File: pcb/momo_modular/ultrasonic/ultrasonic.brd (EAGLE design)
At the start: 100 x 80 mm, 39 parts, among them U1 TDC1000, U2 TDC7200, U3 PIC16LF1847

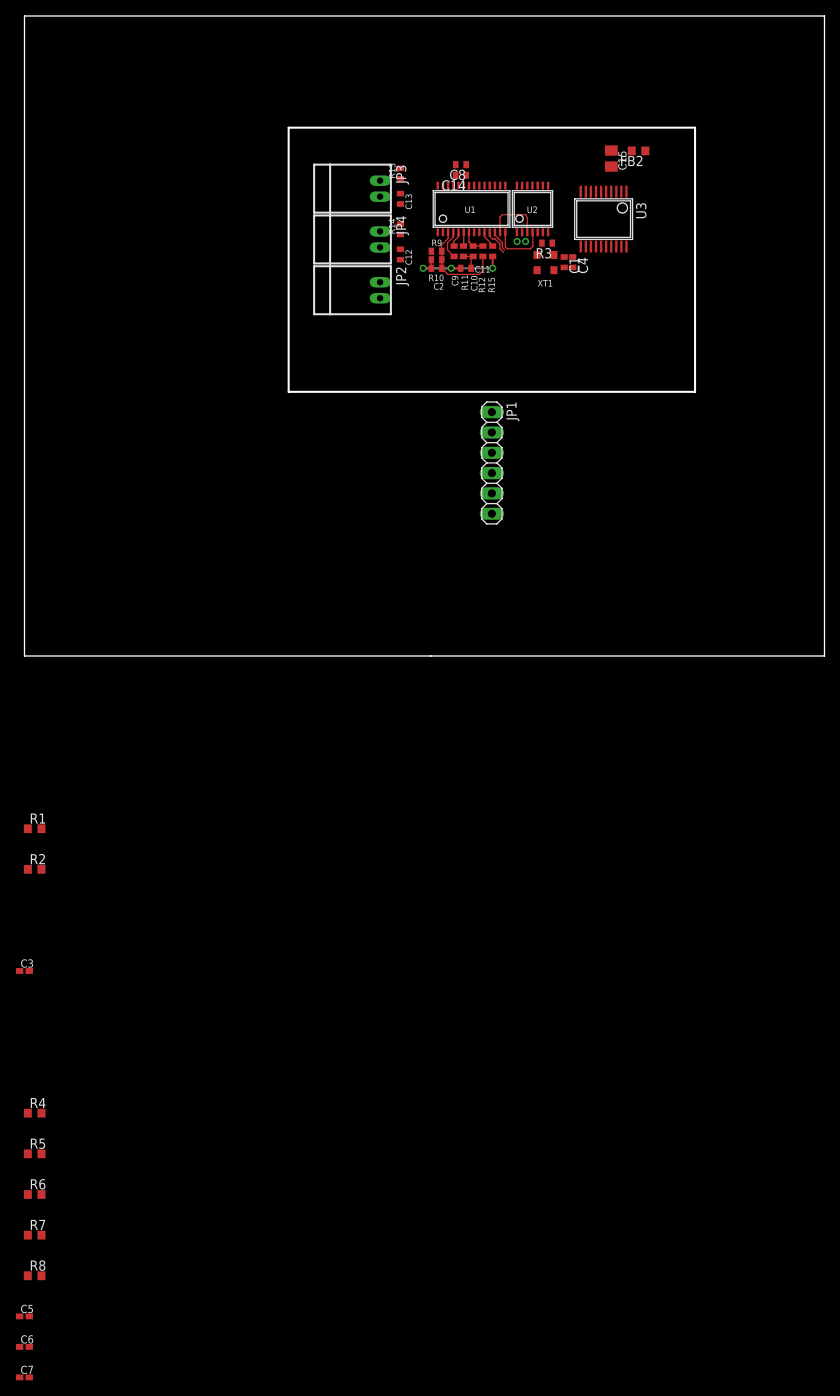
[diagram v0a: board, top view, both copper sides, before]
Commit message: Continue layout of ultrasonic board
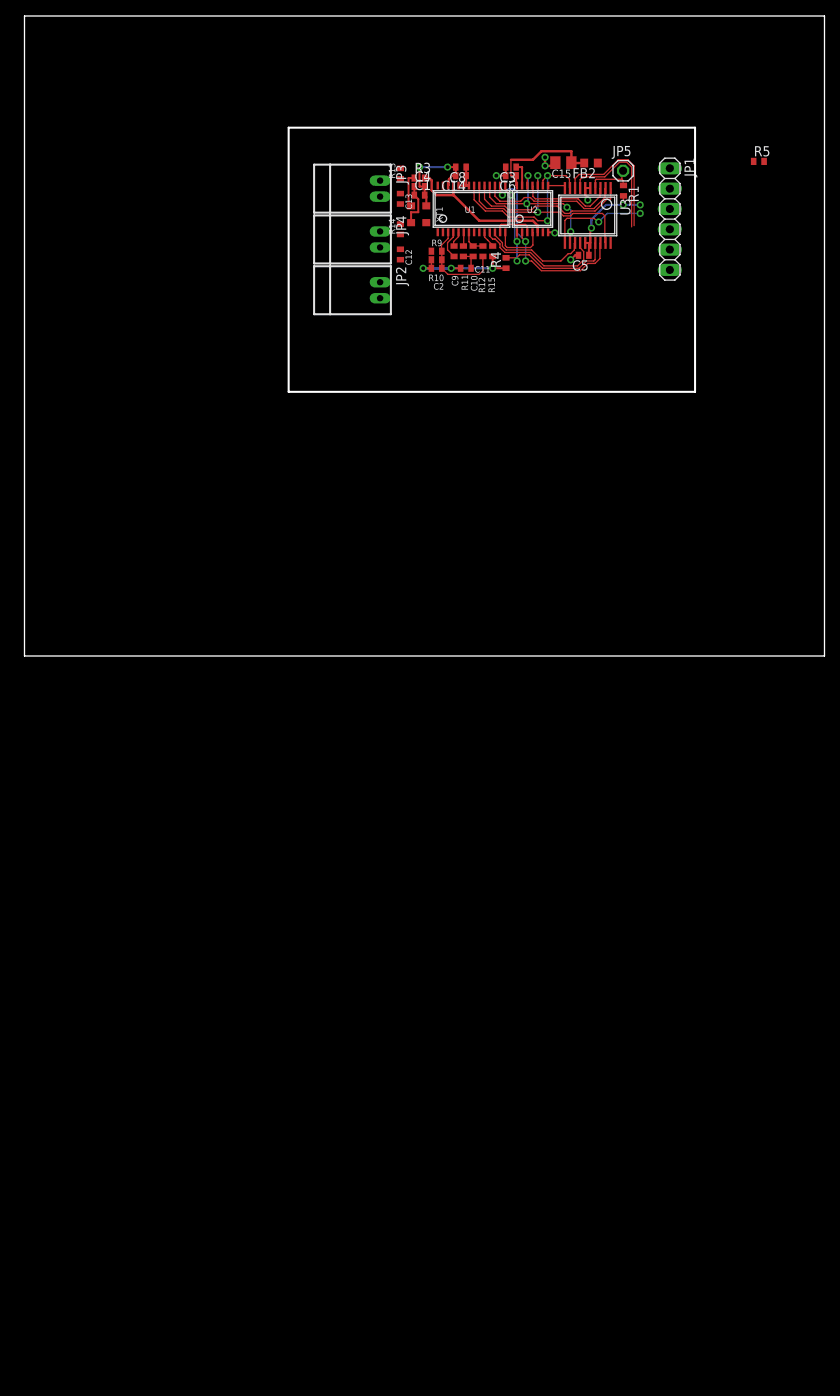
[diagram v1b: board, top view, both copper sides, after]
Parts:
- removed C7: 100 nF, rcl:C0402K
- removed R2, R6, R7, R8: 33R, rcl:R0603
- added JP5: (no value), pinhead:1X01
- C3, C5, C6: device rcl:C0402K -> rcl:C0402
- R1, R4, R5: device rcl:R0603 -> rcl:R0402
- moved C6 158.5 mm to (60.8, 60.0), turned to 180 degrees
- moved R5 153.6 mm to (91.8, 61.8)
- moved C5 149.9 mm to (69.9, 50.1), turned to 180 degrees
- moved R4 121.5 mm to (60.2, 49.1), turned to 90 degrees
- moved C3 117.4 mm to (60.8, 61.1), turned to 180 degrees
- moved R1 108.5 mm to (74.9, 58.2), turned to 270 degrees
- moved JP1 37.7 mm to (80.7, 52.1)
- moved C4 21.4 mm to (49.4, 58.7), turned to 0 degrees
- moved C1 19.9 mm to (49.4, 57.6), turned to 0 degrees
- moved R3 17.9 mm to (49.4, 59.7), turned to 0 degrees
- moved XT1 17.0 mm to (49.3, 55.2), turned to 90 degrees
- moved FB2 6.14 mm to (70.8, 61.6)
- moved C15 6.02 mm to (67.4, 61.7), turned to 180 degrees
- moved U3 2.03 mm to (70.4, 55.1)
- moved C8 0.30 mm to (54.6, 61.1)
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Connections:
- removed net N$1: R2.2, U2.9
- removed net N$22: C1.1, C14.1, C15.1, C4.1, C8.1, FB2.2, U1.22, U1.23, U1.24, XT1.4
- removed net N$5: R6.2, U1.21
- removed net N$7: R7.1, U3.12
- removed net N$8: R8.2, U3.19
- new net VCCINT: C1.1, C14.1, C15.1, C4.1, C6.1, C8.1, FB2.2, U1.22, U1.23, U1.24, U2.14, XT1.4
- net CHSEL: now also U3.14; no longer U3.18
- net CS7200: now also U3.3; no longer U3.2
- net GND: no longer C7.2
- net N$9: now also JP5.1
- net RESET1000: now also U3.2; no longer U3.14
- net SCK: now also U3.12; no longer R7.2
- net SDI: now also U1.21, U2.9; no longer R2.1, R6.1
- net SDO: now also U3.19; no longer R8.1
- net TRIG: now also U3.18; no longer U3.3
- net VCC: no longer C6.1, C7.1, U2.14
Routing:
- net SDO: track 0.00 -> 27.9 mm, vias 0 -> 2
- net ENABLE: track 0.00 -> 26.5 mm, vias 0 -> 3
- net TRIG: track 0.00 -> 26.4 mm, vias 0 -> 3
- net VCCINT: track 0.00 -> 24.5 mm
- net GND: track 16.9 -> 40.8 mm, vias 3 -> 11
- net SDI: track 0.00 -> 23.2 mm, vias 0 -> 2
- net SCK: track 0.00 -> 21.2 mm, vias 0 -> 4
- net CS1000: track 0.00 -> 20.7 mm
- net CLOCK: track 0.00 -> 19.3 mm
- net RESET1000: track 0.00 -> 17.9 mm
- net SDA: track 0.00 -> 17.3 mm
- net ALARM: track 0.00 -> 16.1 mm
- net VCC: track 0.00 -> 13.3 mm, vias 0 -> 3
- net CHSEL: track 3.42 -> 16.6 mm
- net SCL: track 0.00 -> 12.9 mm, vias 0 -> 2
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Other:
- outline, holes or cut-outs redrawn

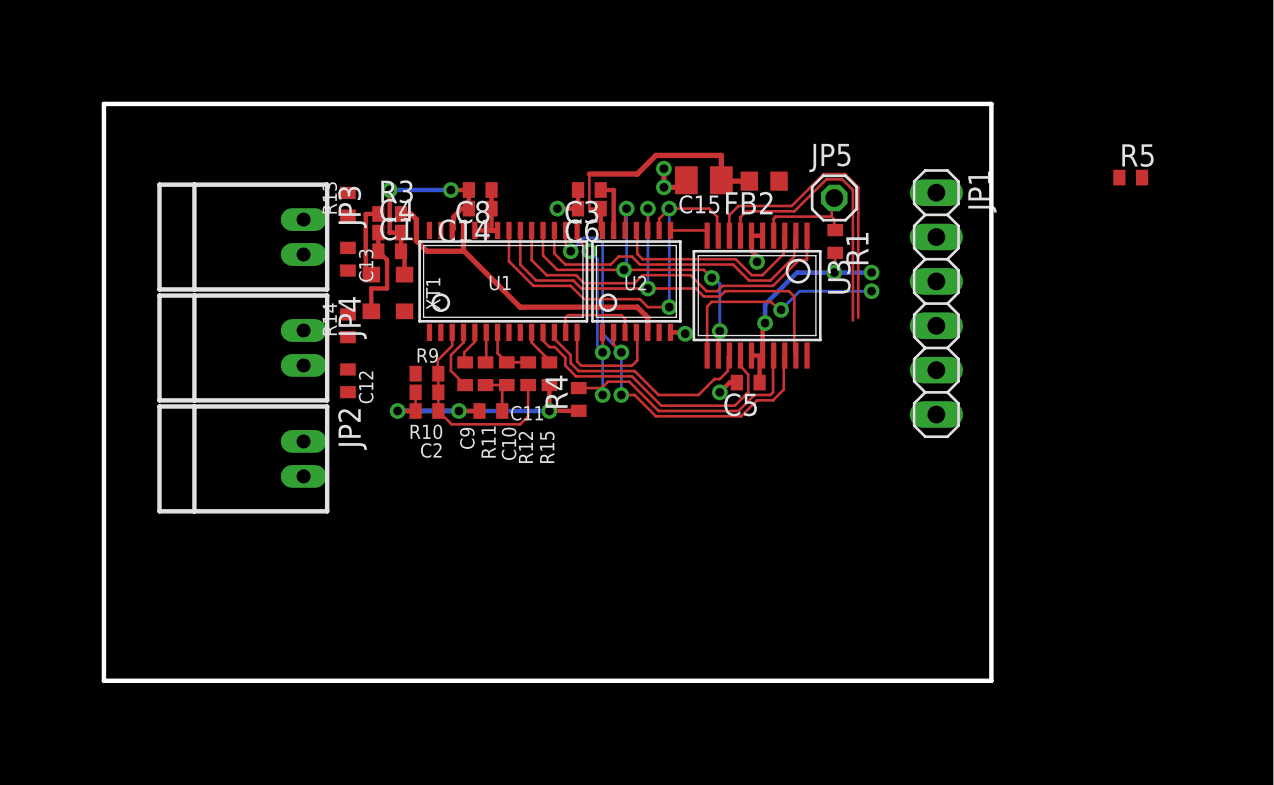
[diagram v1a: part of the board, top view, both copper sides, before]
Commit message: Finish layout of ultrasonic board
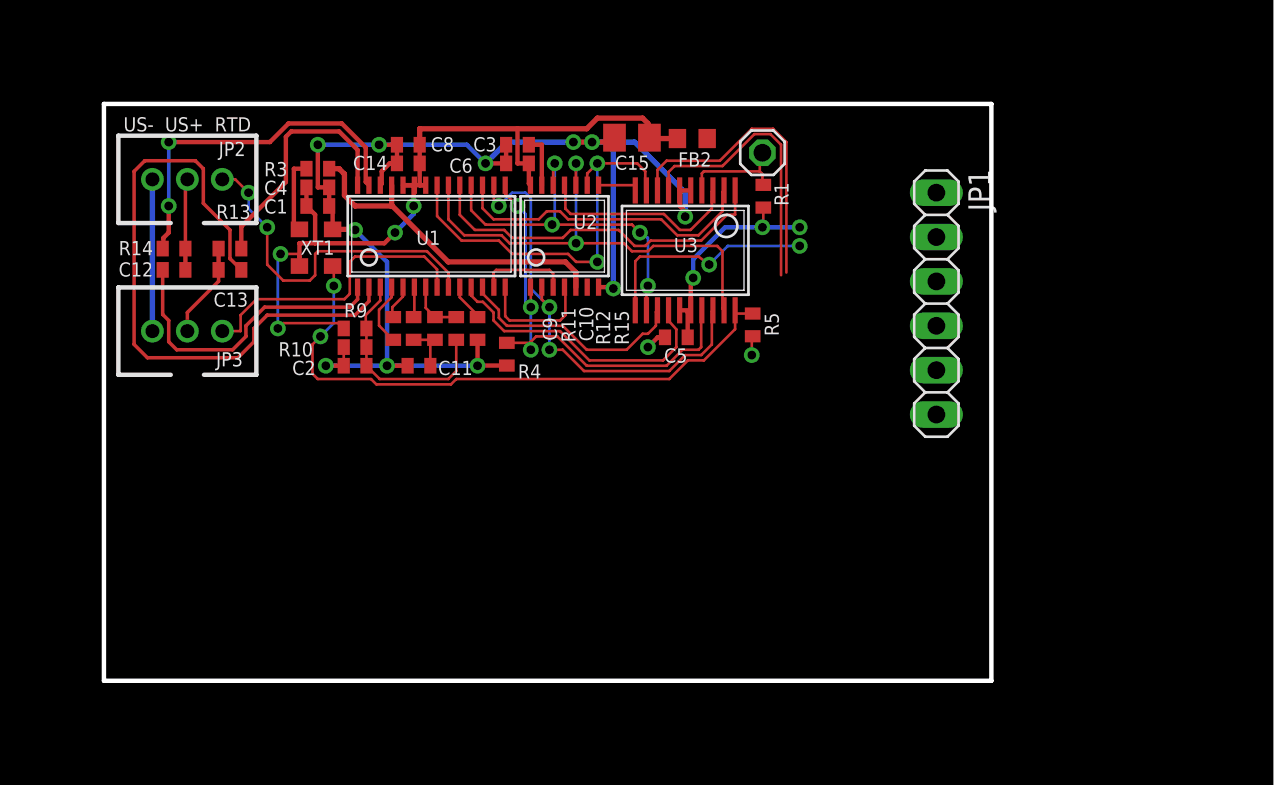
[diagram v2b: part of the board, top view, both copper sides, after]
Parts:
- removed JP4: MOMO-PWR-HOUSED, components:MOMO-PWR-HOUSED
- JP2, JP3: value MOMO-PWR-HOUSED -> JST-PH-3PIN; device components:MOMO-PWR-HOUSED -> custom_ics:JST-PH-3PIN
- moved R5 23.2 mm to (70.2, 53.4), turned to 90 degrees
- moved JP2 17.3 mm to (37.8, 61.7), turned to 0 degrees
- moved C12 11.8 mm to (37.0, 56.5), turned to 180 degrees
- moved R14 10.9 mm to (37.0, 57.8), turned to 180 degrees
- moved JP3 8.56 mm to (37.8, 53.0), turned to 0 degrees
- moved R13 7.22 mm to (40.2, 57.8), turned to 0 degrees
- moved C13 6.78 mm to (40.2, 56.5), turned to 0 degrees
- moved C1 4.86 mm to (45.3, 60.2)
- moved C2 4.86 mm to (47.4, 51.1)
- moved C3 4.86 mm to (56.7, 63.7)
- moved C4 4.86 mm to (45.3, 61.3)
- moved C5 4.86 mm to (65.8, 52.7)
- moved C6 4.86 mm to (56.7, 62.6)
- moved JP5 4.86 mm to (70.7, 63.2)
- moved R1 4.86 mm to (70.8, 60.8)
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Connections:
- new net RTD2: JP2.3, U1.9
- net GND: now also JP2.1, JP3.1; no longer JP2.2, JP3.2, JP4.2
- net N$15: now also JP3.2; no longer JP3.1
- net N$20: now also JP2.2; no longer JP4.1
- net RTD1: now also JP3.3; no longer JP2.1
- net VCC: no longer R9.1
- net VCCINT: now also R9.1
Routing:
- net GND: track 40.8 -> 85.4 mm, vias 11 -> 13
- net N$19: track 0.00 -> 37.4 mm
- net CLKEN: track 0.00 -> 34.6 mm, vias 0 -> 2
- net VCCINT: track 24.5 -> 48.6 mm, vias 0 -> 4
- net N$16: track 0.00 -> 20.8 mm, vias 0 -> 2
- net RTD2: track 0.00 -> 19.9 mm, vias 0 -> 2
- net N$18: track 0.00 -> 17.5 mm
- net RTD1: track 0.00 -> 17.0 mm
- net N$17: track 0.00 -> 14.5 mm
- net N$15: track 0.00 -> 5.47 mm
- net N$20: track 0.00 -> 5.23 mm
- added copper zone on layer 16, net GND
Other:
- board text added: "US- US+ RTD"

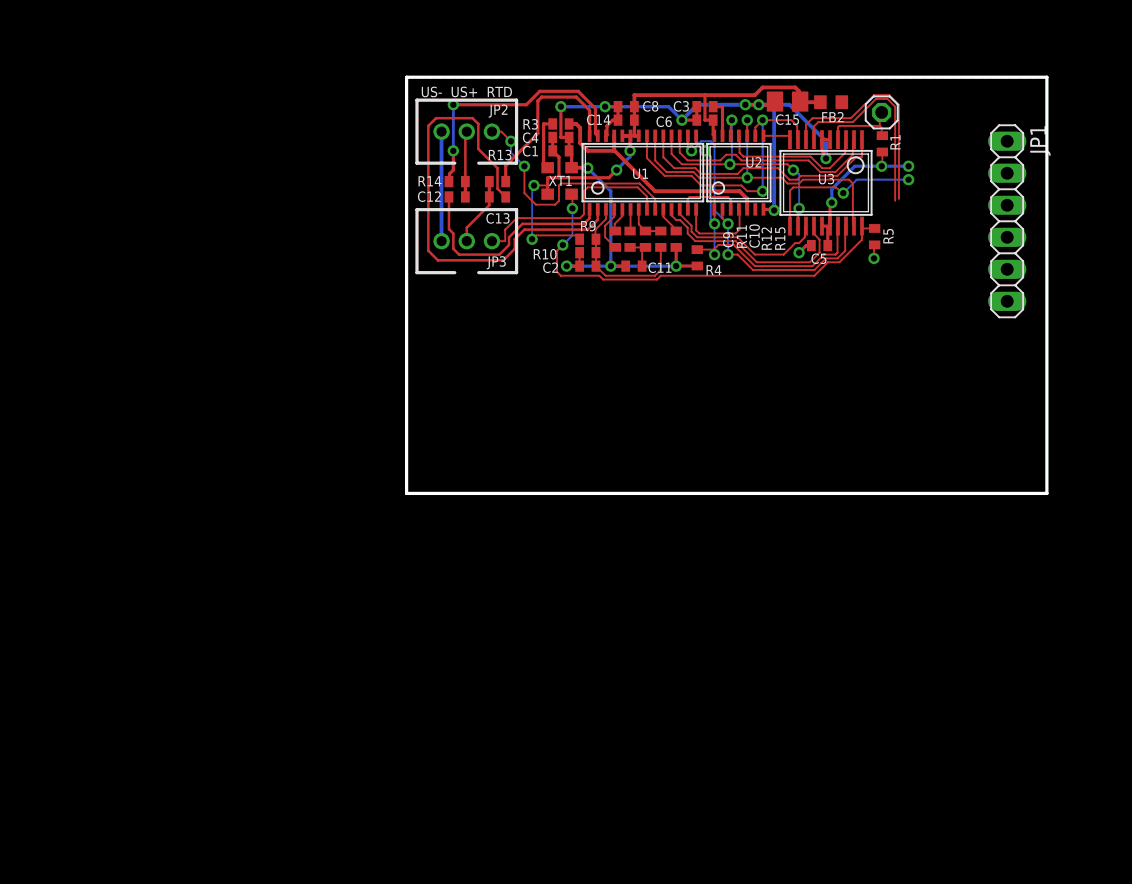
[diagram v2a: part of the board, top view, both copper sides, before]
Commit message: Finish laying out ultrasonic dev board
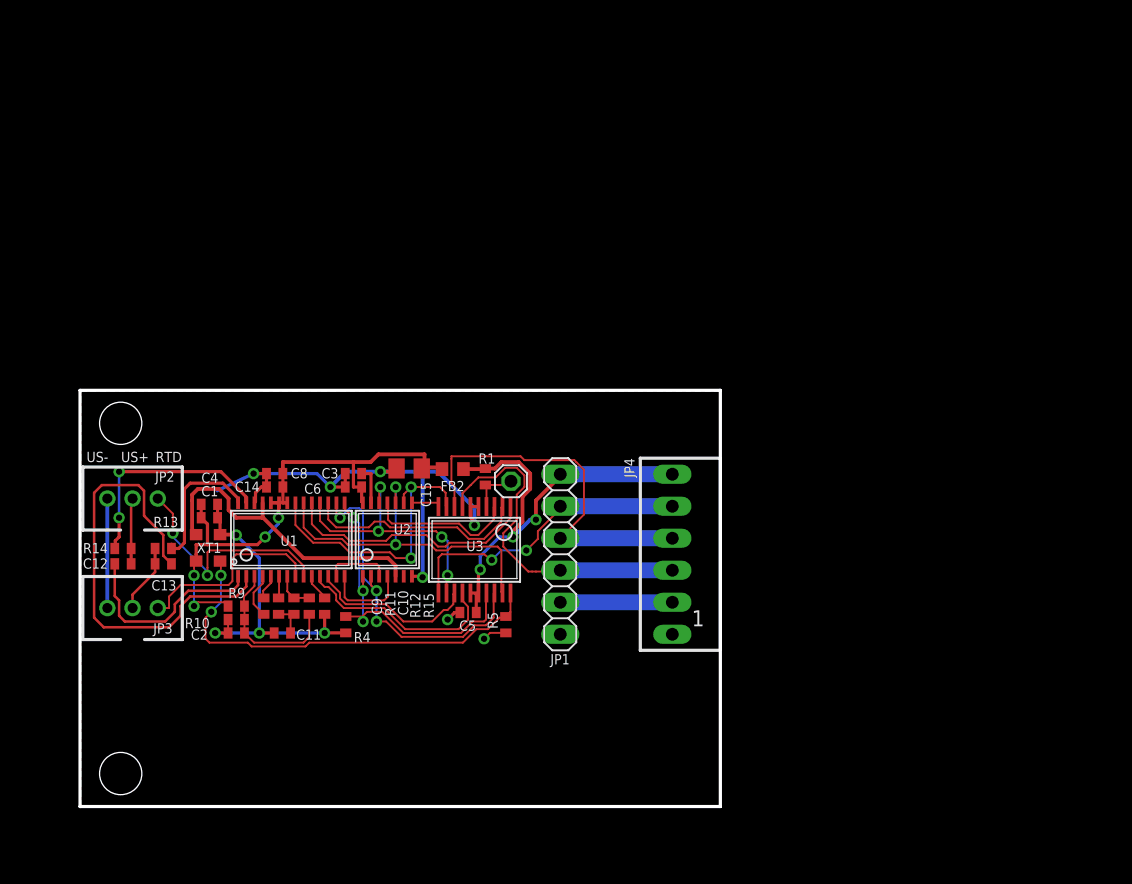
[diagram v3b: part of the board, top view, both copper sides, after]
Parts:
- removed R3: 24.9R, rcl:R0402
- added JP4: MOMO-EDGE-6M-RIGHT, components:MOMO-EDGE-6M
- C10: value 50 pF -> 51 pF
- C11: value 53 pF -> 51 pF
- R12: value 5k -> 5.36k
- moved JP1 44.2 mm to (45.2, 25.7)
- moved R5 42.5 mm to (40.9, 22.6)
- moved C15 41.8 mm to (33.2, 35.0)
- moved FB2 41.8 mm to (36.7, 35.0)
- moved JP5 41.5 mm to (41.3, 34.0)
- moved R1 41.1 mm to (39.3, 34.3), turned to 90 degrees
- moved C10 40.3 mm to (24.1, 24.1)
- moved C11 40.3 mm to (23.2, 21.9)
- moved C14 40.3 mm to (22.6, 33.5)
- moved C8 40.3 mm to (22.6, 34.6)
- moved C9 40.3 mm to (21.7, 24.1)
- moved R11 40.3 mm to (22.9, 24.1)
- moved R12 40.3 mm to (25.3, 24.1)
- moved C1 40.3 mm to (17.4, 31.1)
- moved C2 40.3 mm to (19.5, 21.9)
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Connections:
- removed net N$3: R3.1, XT1.3
- net 4V: now also JP4.CLK
- net ALARM: now also JP4.DAT
- net CLOCK: now also XT1.3; no longer R3.2
- net GND: now also JP4.V28
- net SCL: now also JP4.4V
- net SDA: now also JP4.ALARM
- net VCC: now also JP4.GND
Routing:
- net VCC: track 13.3 -> 35.7 mm
- net SDA: track 17.3 -> 30.1 mm
- net ALARM: track 16.1 -> 27.7 mm
- net SCL: track 12.9 -> 23.9 mm
- net 4V: track 0.00 -> 8.89 mm
- net CLOCK: track 19.3 -> 24.7 mm
- net N$3: track 4.51 -> 0.00 mm
- net VCCINT: track 48.6 -> 44.6 mm
- net N$17: track 14.5 -> 11.2 mm
- net N$16: track 20.8 -> 17.6 mm
- net N$9: track 6.32 -> 3.90 mm
- net GND: track 85.4 -> 84.0 mm, vias 13 -> 11
- net RTD1: track 17.0 -> 15.6 mm
- net N$19: track 37.4 -> 36.0 mm
- net N$18: track 17.5 -> 16.1 mm
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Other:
- outline, holes or cut-outs redrawn
- board text added: "RTD"
- board text added: "US+"
- board text added: "US-"
- board text added: "Ultrasonic Sensor Module Version 1.0 5/7/2015"
- board text removed: "US- US+ RTD"

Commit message: Finish laying out version 1.0 of ultrasonic board
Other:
- board size 100 x 80 mm -> 50.8 x 33 mm
